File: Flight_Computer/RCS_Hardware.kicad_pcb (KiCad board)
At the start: 2 copper layers, 124.3 x 65.3 mm, 89 parts, among them J1 SWD, J10 Motor, J2 TYPE-C-31-M-12, J3 I2C, J4 5V, J5 GND, J6 AMT102, J7 FC_RF, J8 AMT102, Q1 2N7002, Q2 2N7002, Q3 2N7002, Q4 2N7002, Q5 2N7002, Q6 2N7002, U1 STM32F401CCU6, U2 AMS1117-3.3, U3 TMP102xxDRL, U4 BNO055, U5 W25Q32JVSS, U6 LM2576S-5, Y1 16MHz, Y2 32.768Mhz

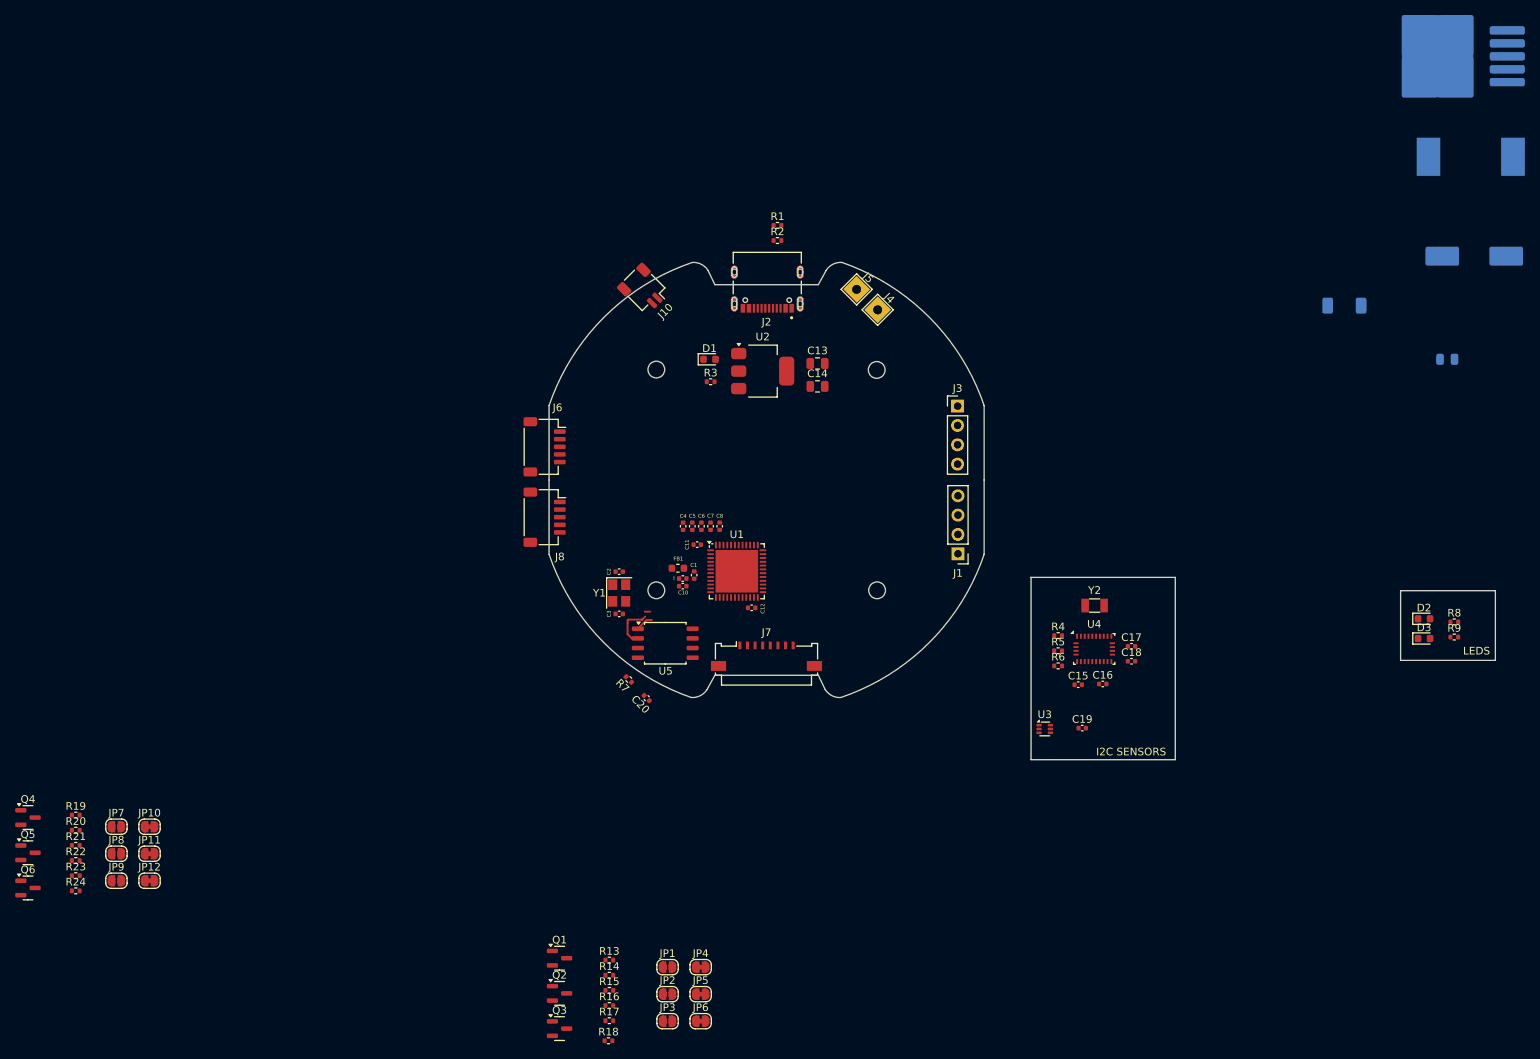
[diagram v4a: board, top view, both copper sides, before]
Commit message: finished (preliminary) placing of gyro pcb components
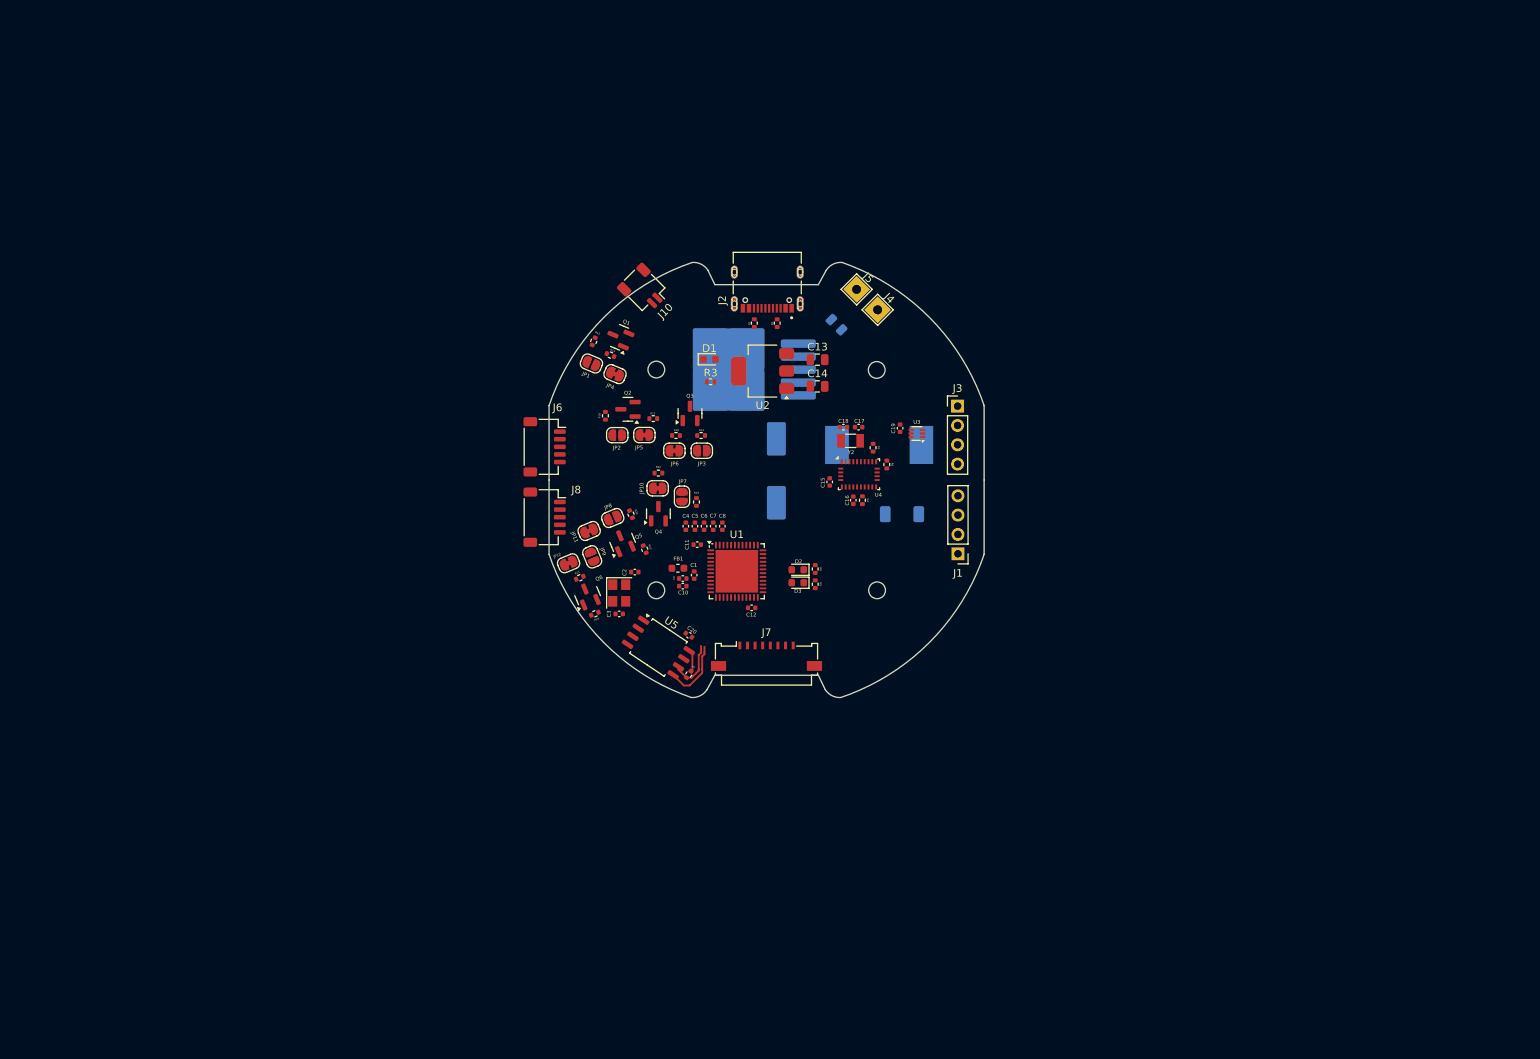
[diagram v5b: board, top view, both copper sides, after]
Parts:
- moved U6 101.8 mm to (151.2, 75.1)
- moved C28 95.9 mm to (156.0, 88.4), turned to 90 degrees
- moved Q4 91.9 mm to (140.5, 94.0), turned to 90 degrees
- moved R22 91.9 mm to (140.5, 88.7)
- moved R19 91.3 mm to (145.5, 92.5), turned to -90 degrees
- moved Q5 88.1 mm to (135.8, 97.8), turned to 112.5 degrees
- moved L1 86.4 mm to (169.5, 85.0)
- moved R23 86.2 mm to (138.7, 98.7), turned to 112.5 degrees
- moved JP7 86.0 mm to (143.6, 91.8), turned to -90 degrees
- moved R15 85.3 mm to (132.0, 71.4), turned to -112.5 degrees
- moved R8 84.2 mm to (161.1, 101.3), turned to -90 degrees
- moved R9 84.2 mm to (161.1, 103.3), turned to 90 degrees
- moved R20 83.9 mm to (136.9, 94.1), turned to 112.5 degrees
- moved Q6 82.9 mm to (131.2, 104.8), turned to 112.5 degrees
- moved Q3 82.6 mm to (144.7, 80.9), turned to 90 degrees
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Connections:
- U1 pad 11: /S1 -> /S1_RF
- U1 pad 12: /RX -> /TX_RADIO
- U1 pad 13: /TX -> /RX_RADIO
- U1 pad 19: /S2 -> /S2_RF
- U1 pad 20: /I2 -> unconnected-(U1-PB2-Pad20)
- U1 pad 21: unconnected-(U1-PB10-Pad21) -> /RADIO_NRST
- U1 pad 26: /S4 -> unconnected-(U1-PB13-Pad26)
- U1 pad 27: /S5 -> unconnected-(U1-PB14-Pad27)
- U1 pad 28: /S6 -> unconnected-(U1-PB15-Pad28)
- U1 pad 31: unconnected-(U1-PA10-Pad31) -> /LED_G
- U1 pad 38: /LED_G -> /PWM
- U1 pad 39: /I1 -> unconnected-(U1-PB3-Pad39)
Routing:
- net /MOSI: track 0.00 -> 8.65 mm
- net /SCLK: track 0.00 -> 7.24 mm
- net /MISO: track 6.65 -> 0.00 mm
- net +3.3V: track 0.00 -> 2.96 mm
- net /CS_FLASH: track 2.32 -> 0.00 mm
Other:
- board size 124.3 x 65.3 mm -> 57.2 x 57.2 mm
- board text added: "C15"
- board text added: "C16"
- board text added: "C17"
- board text added: "C18"
- board text added: "C19"
- board text added: "C20"
- board text added: "D2"
- board text added: "JP10"
- board text added: "JP2"
- board text added: "JP3"
- board text added: "JP5"
- board text added: "JP6"
- board text added: "Q2"
- board text added: "Q3"
- board text added: "R1"
- board text added: "R13"
- board text added: "R14"
- board text added: "R15"
- board text added: "R16"
- board text added: "R17"
- board text added: "R18"
- board text added: "R19"
- board text added: "R2"
- board text added: "R20"
- board text added: "R21"
- board text added: "R22"
- board text added: "R23"
- board text added: "R24"
- board text added: "R4"
- board text added: "R5"
- board text added: "R6"
- board text added: "R7"
- board text added: "R8"
- board text added: "R9"
- board text removed: "I2C SENSORS"
- board text removed: "LEDS"

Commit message: routed pcb
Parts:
- C27: value 150uF -> 100uF
- C28: value 680uF -> 470uF
- L1: value 100uH -> 150uH
- moved G*** 62.8 mm to (260.1, 77.9)
- moved JP11 31.9 mm to (163.2, 93.9), turned to 180 degrees
- moved R7 29.8 mm to (173.6, 108.9), turned to -56.25 degrees
- moved JP8 28.8 mm to (163.1, 91.3), turned to -179.6 degrees
- moved J4 28.5 mm to (140.8, 65.6), turned to -157.5 degrees
- moved U5 28.2 mm to (168.7, 112.0), turned to 33.75 degrees
- moved JP2 28.1 mm to (163.2, 84.2)
- moved C20 28.0 mm to (172.4, 107.2), turned to -56.25 degrees
- moved R16 27.2 mm to (160.6, 84.0)
- moved JP12 24.8 mm to (152.8, 94.3), turned to 180 degrees
- moved JP5 24.7 mm to (163.2, 86.8), turned to 180 degrees
- moved R20 24.0 mm to (160.7, 91.0), turned to -90 degrees
- moved C15 22.9 mm to (164.0, 67.0), turned to 67.5 degrees
- moved R21 22.8 mm to (150.1, 91.4), turned to -90 degrees
- moved Q5 22.7 mm to (157.8, 92.5), turned to 179.2 degrees
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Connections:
- J3 pad 1: /VCC -> +3.3V
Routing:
- net +3.3V: track 2.96 -> 285.7 mm, vias 0 -> 14
- net +5V: track 0.00 -> 161.1 mm, vias 0 -> 5
- net GND: track 0.00 -> 100.3 mm, vias 0 -> 42
- net /PWM: track 0.00 -> 90.2 mm, vias 0 -> 4
- net +BATT: track 0.00 -> 87.2 mm
- net /USB_D+: track 0.00 -> 69.5 mm, vias 0 -> 6
- net /USB_D-: track 0.00 -> 68.5 mm, vias 0 -> 4
- net /SDA: track 0.00 -> 61.6 mm
- net /SCL: track 0.00 -> 60.6 mm, vias 0 -> 2
- net /BNO_NRST: track 0.00 -> 52.6 mm
- net /NRST: track 0.00 -> 44.4 mm, vias 0 -> 2
- net Net-(J6-Pin_4): track 0.00 -> 39.1 mm, vias 0 -> 2
- net Net-(J8-Pin_4): track 0.00 -> 38.6 mm, vias 0 -> 2
- net /E1A: track 0.00 -> 33.4 mm, vias 0 -> 2
- net Net-(J8-Pin_5): track 0.00 -> 27.4 mm
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- added copper zone on B.Cu, net GND
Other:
- board text removed: "C10"
- board text removed: "C11"
- board text removed: "C15"
- board text removed: "C16"
- board text removed: "C17"
- board text removed: "C18"
- board text removed: "C19"
- board text removed: "C2"
- board text removed: "C20"
- board text removed: "C3"
- board text removed: "C4"
- board text removed: "C5"
- board text removed: "C6"
- board text removed: "C8"
- board text removed: "C9"
- board text removed: "JP10"
- board text removed: "JP2"
- board text removed: "JP3"
- board text removed: "JP5"
- board text removed: "JP6"
- board text removed: "Q2"
- board text removed: "Q3"
- board text removed: "R1"
- board text removed: "R13"
- board text removed: "R14"
- board text removed: "R15"
- board text removed: "R16"
- board text removed: "R17"
- board text removed: "R18"
- board text removed: "R19"
- board text removed: "R2"
- board text removed: "R20"
- board text removed: "R21"
- board text removed: "R22"
- board text removed: "R23"
- board text removed: "R24"
- board text removed: "R4"
- board text removed: "R5"
- board text removed: "R6"
- board text removed: "R7"

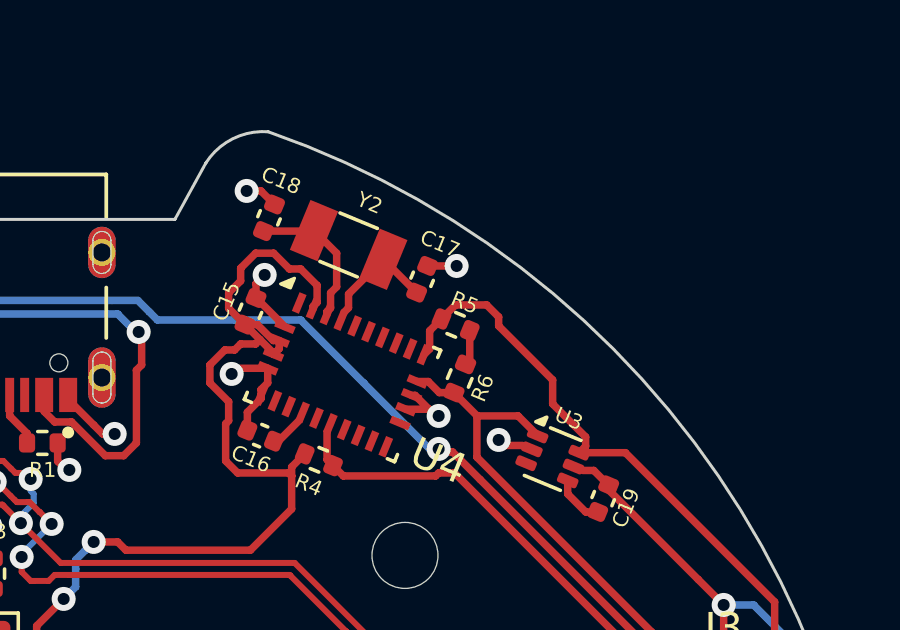
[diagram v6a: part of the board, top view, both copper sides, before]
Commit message: added part numbers for some footprints on pcb
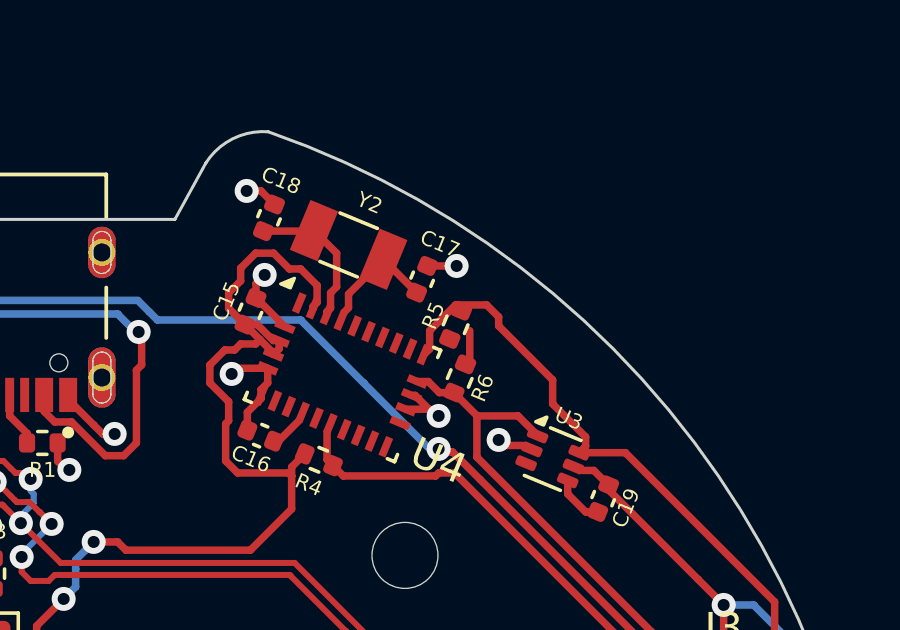
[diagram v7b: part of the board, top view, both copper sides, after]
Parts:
- Y2: value 32.768Mhz -> 32.768Khz
- turned R5 to -112.5 degrees
